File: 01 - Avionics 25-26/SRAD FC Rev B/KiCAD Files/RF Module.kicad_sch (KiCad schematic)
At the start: 11 parts, among them U7 SX1276IMLTRT, Y2 Crystal_GND2 (32 MHz)

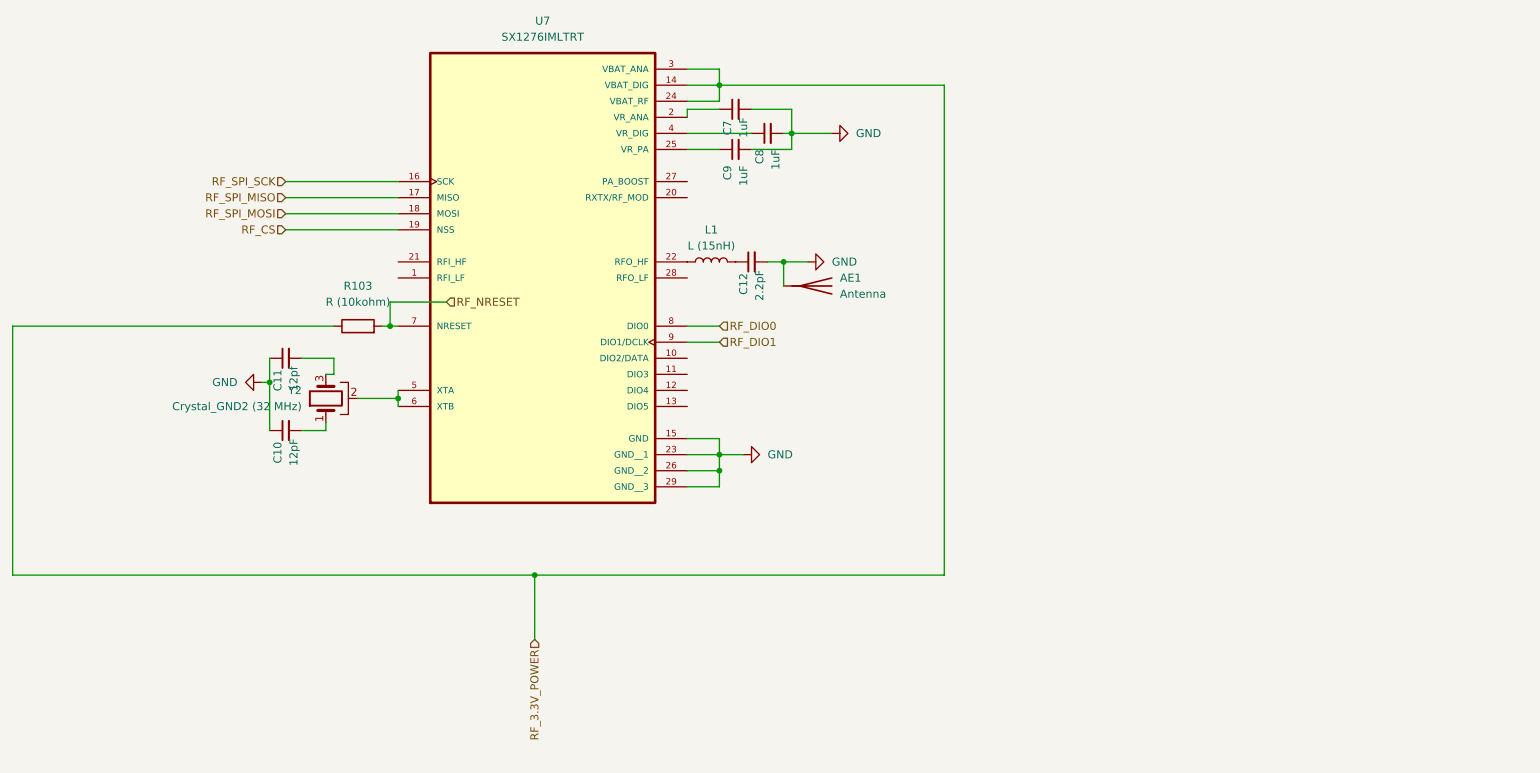
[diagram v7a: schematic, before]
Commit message: switched to RA-01H
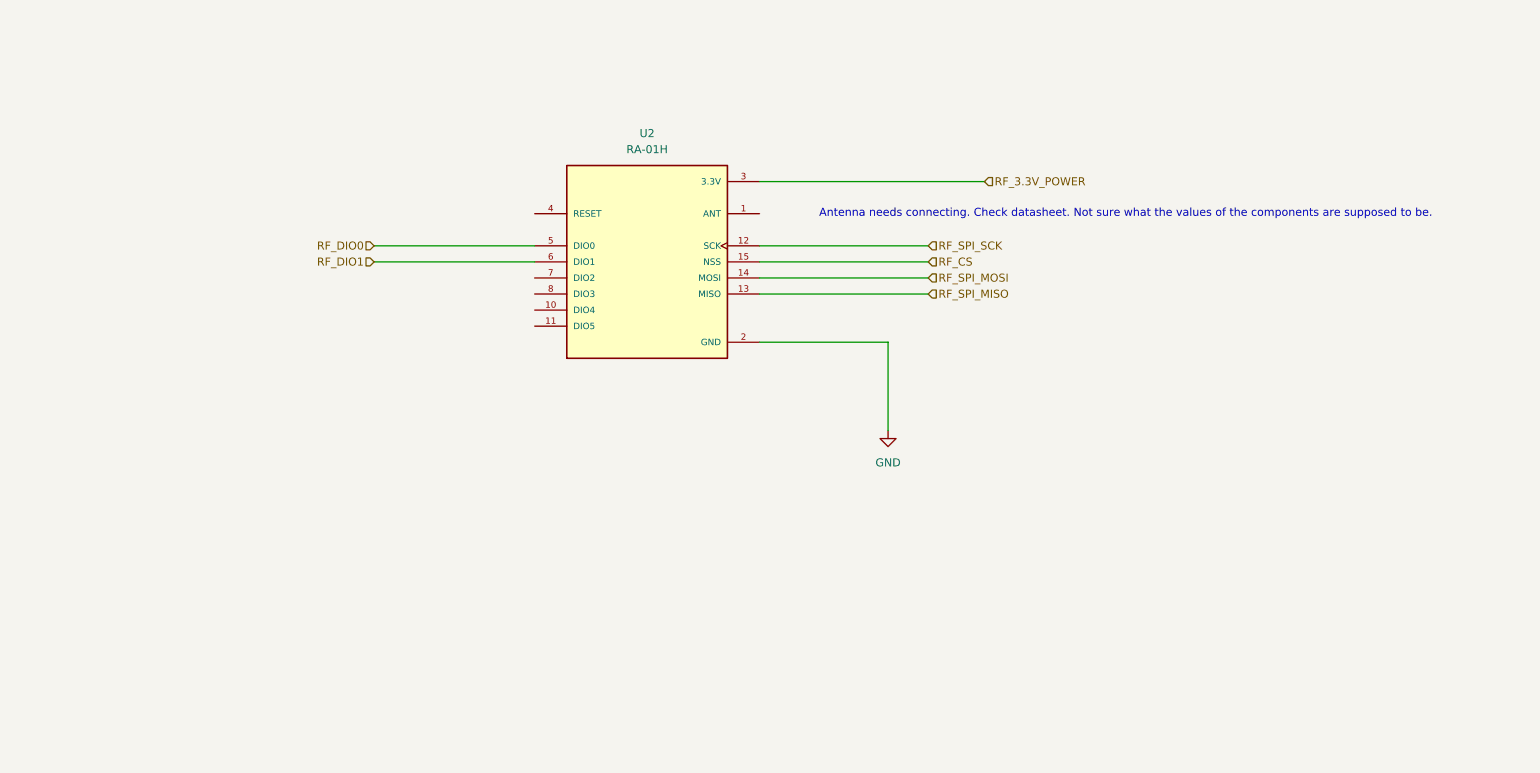
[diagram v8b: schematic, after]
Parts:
- removed AE1: Antenna, symbol Device:Antenna
- removed C10: 12pF, symbol Device:C_Small
- removed C11: 12pf, symbol Device:C_Small
- removed C12: 2.2pF, symbol Device:C_Small
- removed C7, C8, C9: 1uF, symbol Device:C_Small
- removed L1: L (15nH), symbol Device:L
- removed R103: R (10kohm), symbol Device:R
- removed U7: SX1276IMLTRT, SX1276IMLTRT:QFN65P600X600X100-29N, symbol SX1276IMLTRT:SX1276IMLTRT
- removed Y2: Crystal_GND2 (32 MHz), symbol Device:Crystal_GND2
- added U2: RA-01H, RA-01H:XCVR_RA-01H, symbol RA-01H:RA-01H
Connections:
- net GND: now also U2.16 (GND), U2.2 (GND), U2.9 (GND)
- net RF_3.3V_POWER: now also U2.3 (3.3V)
- net RF_CS: now also U2.15 (NSS)
- net RF_DIO0: now also U2.5 (DIO0)
- net RF_DIO1: now also U2.6 (DIO1)
- net RF_SPI_MISO: now also U2.13 (MISO)
- net RF_SPI_MOSI: now also U2.14 (MOSI)
- net RF_SPI_SCK: now also U2.12 (SCK)
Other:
- note added: "Antenna needs connecting. Check datasheet. Not sure what the values of the components are supposed to be."
